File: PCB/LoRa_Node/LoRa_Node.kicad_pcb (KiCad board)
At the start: 2 copper layers, 90 x 34 mm, 65 parts, among them IC1 SPX5205M5-L/TR, IC2 SPX5205M5-L/TR, J1 Conn_01x04_Socket, J2 Conn_01x02_Pin, J3 UF.L, J4 2x5_2.00mm, J6 Conn_01x06_Socket, J7 Conn_01x03_Socket, SW1 SW_SPST, U1 BME280, U2 RFM95W-868S2, U3 STM32F103C8Tx, U4 SIM800L-CORE, Y1 12MHz, Y2 32.768kHz

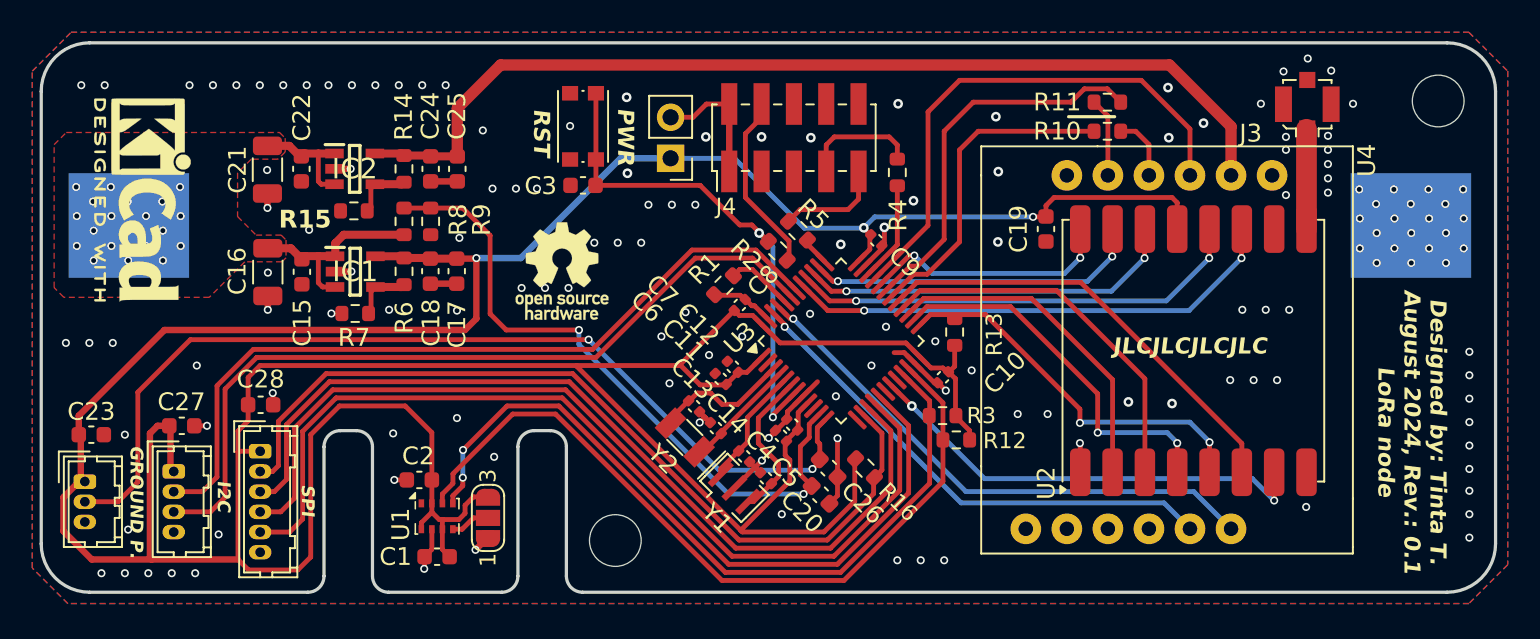
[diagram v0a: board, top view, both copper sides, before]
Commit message: Update
PCB: added pull-downs on IRQ pins, SW: stable EXTI, reliable measurements
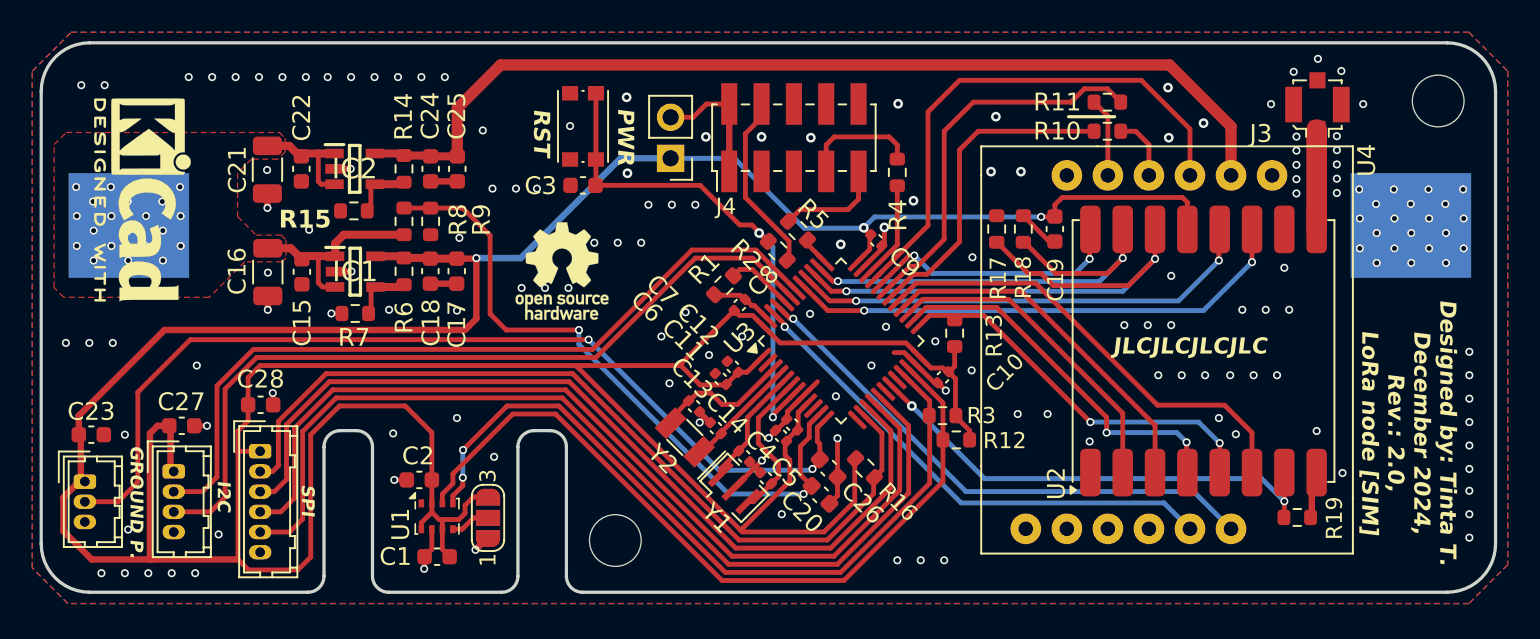
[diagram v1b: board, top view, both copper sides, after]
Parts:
- added R17: 10k, Resistor_SMD:R_0603_1608Metric, F.Cu at (164.8, 77.2)
- added R18: 10k, Resistor_SMD:R_0603_1608Metric, F.Cu at (166.5, 77.2)
- added R19: 10k, Resistor_SMD:R_0603_1608Metric, F.Cu at (183.4, 95.1)
- moved J3 0.63 mm to (184.7, 69.5)
- moved U2 0.63 mm to (177.6, 84.8)
- moved C19 0.55 mm to (168.4, 77.2)
- moved R13 0.08 mm to (162.2, 83.7)
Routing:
- net /DIO0: track 23.6 -> 35.2 mm
- net /DIO1: track 20.8 -> 28.2 mm
- net GND: track 41.3 -> 45.1 mm, vias 149 -> 161
- net /MOSI: track 23.5 -> 21.7 mm
- net /MISO: track 20.8 -> 19.6 mm
- net /DIO5: track 28.4 -> 29.6 mm
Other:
- board text added: "Designed by: Tinta T. December 2024, Rev.: 2.0, LoRa node [SIM]"
- board text removed: "Designed by: Tinta T. August 2024, Rev.: 0.1 LoRa node"

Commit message: Update
Humidity probe is rewired from the 3v3 to MCU pin for power
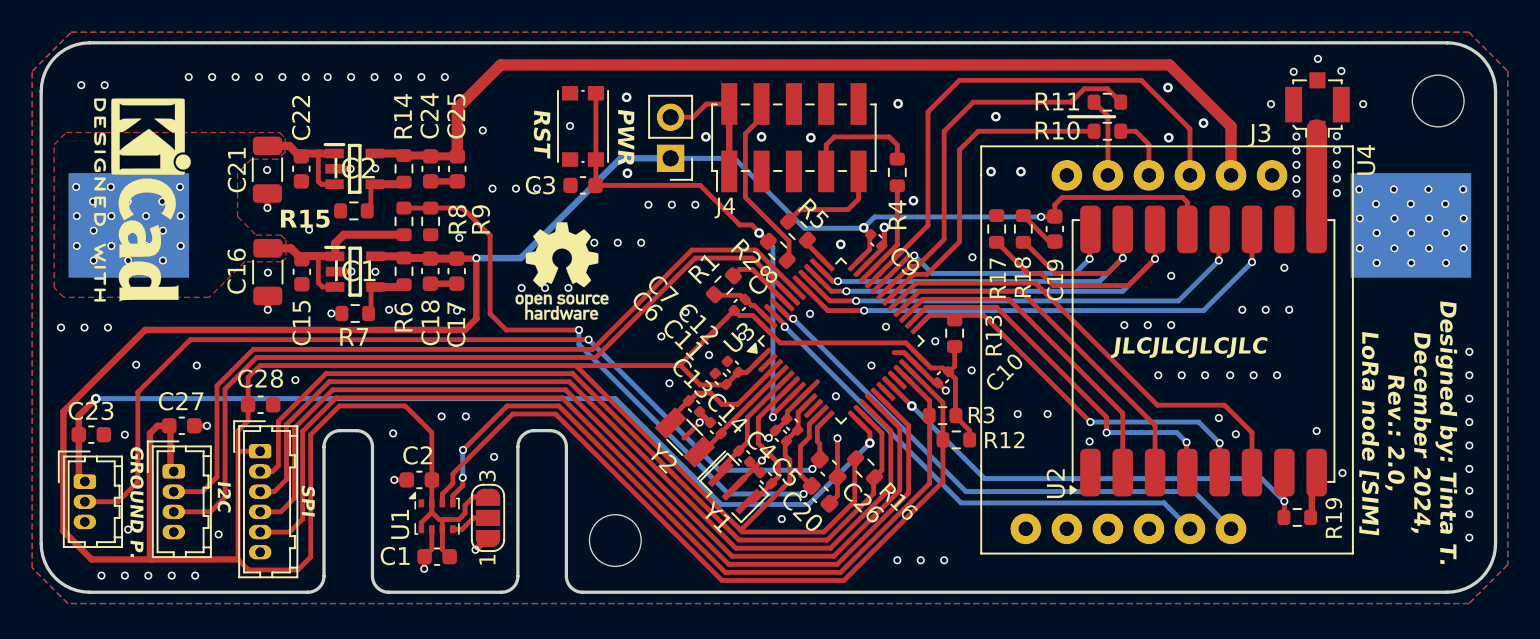
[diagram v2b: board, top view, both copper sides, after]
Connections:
- C23 pad 1: +3.3V -> /EHUM_PWR
- J7 pad 1: +3.3V -> /EHUM_PWR
- U3 pad 13: unconnected-(U3-PA3-Pad13) -> /EHUM_PWR
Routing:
- net /EHUM_PWR: track 0.00 -> 60.4 mm, vias 0 -> 2
- net GND: track 45.1 -> 45.8 mm, vias 161 -> 165

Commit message: README Update
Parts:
- added R20: 10k, Resistor_SMD:R_0603_1608Metric, F.Cu at (108.8, 88.4)
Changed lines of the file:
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@@
 		(tags "capacitor")
 		(property "Reference" "C23"
-			(at 0 -1.43 0)
+			(at -0.02132 -2.978681 0)
 			(layer "F.SilkS")
 			(effects
@@
 		)
 	)
+	(footprint "Resistor_SMD:R_0603_1608Metric"
+		(layer "F.Cu")
+		(at 108.77868 88.421319)
+		(descr "Resistor SMD 0603 (1608 Metric), square (rectangular) end terminal, IPC_7351 nominal, (Body size source: IPC-SM-782 page 72, https://www.pcb-3d.com/wordpress/wp-content/uploads/ipc-sm-782a_amendment_1_and_2.pdf), generated with kicad-footprint-generator")
+		(tags "resistor")
+		(property "Reference" "R20"
+			(at -0.1 -2.8 0)
+			(layer "F.SilkS")
+			(effects
+				(font
+					(size 1 1)
+					(thickness 0.15)
+				)
+			)
+		)
+		(property "Value" "10k"
+			(at 0 1.43 0)
+			(layer "F.Fab")
+			(effects
+				(font
+					(size 1 1)
+					(thickness 0.15)
+				)
+			)
+		)
+		(property "Footprint" "Resistor_SMD:R_0603_1608Metric"
+			(at 0 0 0)
+			(unlocked yes)
+			(layer "F.Fab")
+			(hide yes)
+			(effects
+				(font
+					(size 1.27 1.27)
+				)
+			)
+		)
+		(property "Datasheet" ""
+			(at 0 0 0)
+			(unlocked yes)
+			(layer "F.Fab")
+			(hide yes)
+			(effects
+				(font
+					(size 1.27 1.27)
+				)
+			)
+		)
+		(property "Description" ""
+			(at 0 0 0)
+			(unlocked yes)
+			(layer "F.Fab")
+			(hide yes)
+			(effects
+				(font
+					(size 1.27 1.27)
+				)
+			)
+		)
+		(property ki_fp_filters "R_*")
+		(sheetname "Root")
+		(sheetfile "LoRa_Node.kicad_sch")
+		(attr smd)
+		(fp_line
+			(start -0.237258 -0.5225)
+			(end 0.237258 -0.5225)
+			(stroke
+				(width 0.12)
+				(type solid)
+			)
+			(layer "F.SilkS")
+		)
+		(fp_line
+			(start -0.237258 0.5225)
+			(end 0.237258 0.5225)
+			(stroke
+				(width 0.12)
+				(type solid)
+			)
+			(layer "F.SilkS")
+		)
+		(fp_line
+			(start -1.48 -0.73)
+			(end 1.48 -0.73)
+			(stroke
+				(width 0.05)
+				(type solid)
+			)
+			(layer "F.CrtYd")
+		)
+		(fp_line
+			(start -1.48 0.73)
+			(end -1.48 -0.73)
+			(stroke
+				(width 0.05)
+				(type solid)
+			)
+			(layer "F.CrtYd")
+		)
+		(fp_line
+			(start 1.48 -0.73)
+			(end 1.48 0.73)
+			(stroke
+				(width 0.05)
+				(type solid)
+			)
+			(layer "F.CrtYd")
+		)
+		(fp_line
+			(start 1.48 0.73)
+			(end -1.48 0.73)
+			(stroke
+				(width 0.05)
+				(type solid)
+			)
+			(layer "F.CrtYd")
+		)
+		(fp_line
+			(start -0.8 -0.4125)
+			(end 0.8 -0.4125)
+			(stroke
+				(width 0.1)
+				(type solid)
+			)
+			(layer "F.Fab")
+		)
+		(fp_line
+			(start -0.8 0.4125)
+			(end -0.8 -0.4125)
+			(stroke
+				(width 0.1)
+				(type solid)
+			)
+			(layer "F.Fab")
+		)
+		(fp_line
+			(start 0.8 -0.4125)
+			(end 0.8 0.4125)
+			(stroke
+				(width 0.1)
+				(type solid)
+			)
+			(layer "F.Fab")
+		)
+		(fp_line
+			(start 0.8 0.4125)
+			(end -0.8 0.4125)
+			(stroke
+				(width 0.1)
+				(type solid)
+			)
+			(layer "F.Fab")
+		)
+		(fp_text user "${REFERENCE}"
+			(at 0 0 0)
+			(layer "F.Fab")
+			(effects
+				(font
+					(size 0.4 0.4)
+					(thickness 0.06)
+				)
+			)
+		)
+		(pad "1" smd roundrect
+			(at -0.825 0)
+			(size 0.8 0.95)
+			(layers "F.Cu" "F.Paste" "F.Mask")
+			(roundrect_rratio 0.25)
+			(net 62 "/EHUM_PWR")
+			(pintype "passive")
+		)
+		(pad "2" smd roundrect
+			(at 0.825 0)
+			(size 0.8 0.95)
+			(layers "F.Cu" "F.Paste" "F.Mask")
+			(roundrect_rratio 0.25)
+			(net 1 "GND")
+			(pintype "passive")
+		)
+		(model "${KICAD8_3DMODEL_DIR}/Resistor_SMD.3dshapes/R_0603_1608Metric.wrl"
+			(offset
+				(xyz 0 0 0)
+			)
+			(scale
+				(xyz 1 1 1)
+			)
+			(rotate
+				(xyz 0 0 0)
+			)
+		)
+	)
 	(footprint "Capacitor_SMD:C_0402_1005Metric"
 		(layer "F.Cu")
@@
 	)
 	(via
-		(at 109.82868 83.321319)
+		(at 109.67868 82.921319)
 		(size 0.5)
 		(drill 0.3)
@@
 	)
 	(via
-		(at 161.57868 97.721319)
+		(at 162.22868 97.271319)
 		(size 0.5)
 		(drill 0.3)
@@
 	)
 	(via
-		(at 106.92868 83.321319)
+		(at 106.77868 82.921319)
 		(size 0.5)
 		(drill 0.3)
@@
 	)
 	(via
-		(at 158.67868 97.721319)
+		(at 159.32868 97.271319)
 		(size 0.5)
 		(drill 0.3)
@@
 	)
 	(via
-		(at 160.12868 97.721319)
+		(at 160.77868 97.271319)
 		(size 0.5)
 		(drill 0.3)
@@
 	)
 	(via
-		(at 136.37868 74.721319)
+		(at 134.82868 71.121319)
 		(size 0.5)
 		(drill 0.3)
@@
 	)
 	(via
-		(at 108.37868 83.321319)
+		(at 108.22868 82.921319)
 		(size 0.5)
 		(drill 0.3)
@@
 	)
 	(via
-		(at 133.62868 74.721319)
+		(at 134.82868 73.871319)
 		(size 0.5)
 		(drill 0.3)
@@
 	)
 	(via
-		(at 135.07868 74.721319)
+		(at 134.82868 72.421319)
 		(size 0.5)
 		(drill 0.3)
@@
 	)
 	(segment
-		(start 107.07868 88.521319)
-		(end 112.12868 83.471319)
-		(width 0.4)
-		(layer "F.Cu")
-		(net 5)
-	)
-	(segment
 		(start 168.42868 75.721319)
 		(end 168.42868 76.446319)
@@
 	)
 	(segment
+		(start 112.52868 97.671319)
+		(end 108.82868 97.671319)
+		(width 0.4)
+		(layer "F.Cu")
+		(net 5)
+	)
+	(segment
 		(start 118.47868 88.125)
 		(end 118.50368 88.1)
@@
 	)
 	(segment
+		(start 111.27868 83.471319)
+		(end 131.92868 83.471319)
+		(width 0.4)
+		(layer "F.Cu")
+		(net 5)
+	)
+	(segment
 		(start 129.225 95.8)
 		(end 129.225 95.4)
@@
 	)
 	(segment
+		(start 108.82868 97.671319)
+		(end 107.07868 95.921319)
+		(width 0.4)
+		(layer "F.Cu")
+		(net 5)
+	)
+	(segment
 		(start 148.899857 82.571319)
 		(end 149.732231 82.571319)
@@
 	)
 	(segment
-		(start 132.62868 82.771319)
-		(end 132.62868 79.021319)
-		(width 0.4)
-		(layer "F.Cu")
-		(net 5)
-	)
-	(segment
-		(start 107.07868 95.921319)
-		(end 107.07868 88.521319)
+		(start 131.92868 83.471319)
+		(end 132.62868 82.771319)
 		(width 0.4)
 		(layer "F.Cu")
@@
 	)
 	(segment
+		(start 107.07868 95.921319)
+		(end 107.07868 87.671319)
+		(width 0.4)
+		(layer "F.Cu")
+		(net 5)
+	)
+	(segment
 		(start 156.60368 77.196319)
 		(end 157.039269 77.631908)
@@
 	)
 	(segment
-		(start 112.52868 97.671319)
-		(end 108.82868 97.671319)
-		(width 0.4)
-		(layer "F.Cu")
-		(net 5)
-	)
-	(segment
 		(start 152.489411 89.639411)
 		(end 151.739411 90.389411)
@@
 	)
 	(segment
+		(start 107.07868 87.671319)
+		(end 111.27868 83.471319)
+		(width 0.4)
+		(layer "F.Cu")
+		(net 5)
+	)
+	(segment
 		(start 152.02868 91.521319)
 		(end 152.02868 92.821319)
@@
 	)
 	(segment
-		(start 131.92868 83.471319)
-		(end 132.62868 82.771319)
+		(start 132.62868 82.771319)
+		(end 132.62868 79.021319)
 		(width 0.4)
 		(layer "F.Cu")
@@
 	)
 	(segment
-		(start 108.82868 97.671319)
-		(end 107.07868 95.921319)
-		(width 0.4)
-		(layer "F.Cu")
-		(net 5)
-	)
-	(segment
 		(start 176.62868 75.571319)
 		(end 176.32868 75.271319)
@@
 	)
 	(segment
-		(start 112.12868 83.471319)
-		(end 131.92868 83.471319)
-		(width 0.4)
-		(layer "F.Cu")
-		(net 5)
-	)
-	(segment
 		(start 148.589269 82.260731)
 		(end 148.899857 82.571319)
@@
 	)
 	(segment
-		(start 156.97868 90.471319)
-		(end 156.97868 89.821318)
-		(width 0.3)
+		(start 108.57868 87.621319)
+		(end 108.025 88.174999)
+		(width 0.4)
 		(layer "F.Cu")
 		(net 62)
 	)
 	(segment
-		(start 108.025 88.774999)
-		(end 108.025 89.95)
-		(width 0.4)
+		(start 156.97868 90.471319)
+		(end 156.97868 89.821318)
+		(width 0.3)
 		(layer "F.Cu")
 		(net 62)
 	)
 	(segment
-		(start 109.07868 87.721319)
-		(end 108.025 88.774999)
+		(start 108.02868 92.47868)
+		(end 108.02868 89.95368)
 		(width 0.4)
 		(layer "F.Cu")
@@
 	)
 	(segment
-		(start 108.02868 92.47868)
-		(end 108.02868 89.95368)
+		(start 108.025 88.174999)
+		(end 108.025 89.95)
 		(width 0.4)
 		(layer "F.Cu")
@@
 	)
 	(via
-		(at 109.07868 87.721319)
+		(at 108.57868 87.621319)
 		(size 0.6)
 		(drill 0.3)
@@
 	)
 	(segment
-		(start 109.07868 87.721319)
-		(end 141.22868 87.721319)
+		(start 141.12868 87.621319)
+		(end 147.77868 94.271319)
 		(width 0.3)
 		(layer "B.Cu")
@@
 	)
 	(segment
-		(start 153.17868 94.271319)
-		(end 156.97868 90.471319)
+		(start 108.57868 87.621319)
+		(end 141.12868 87.621319)
 		(width 0.3)
 		(layer "B.Cu")
@@
 	)
 	(segment
-		(start 141.22868 87.721319)
-		(end 147.77868 94.271319)
+		(start 153.17868 94.271319)
+		(end 156.97868 90.471319)
 		(width 0.3)
 		(layer "B.Cu")

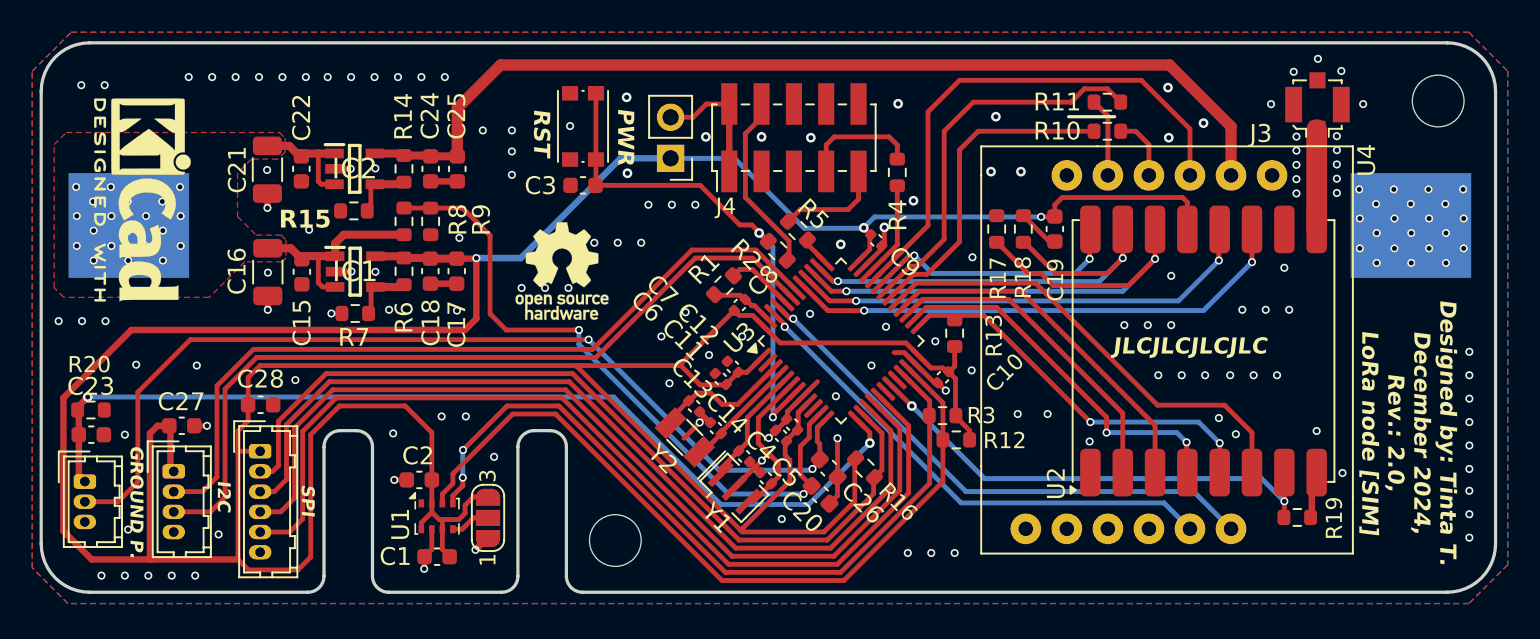
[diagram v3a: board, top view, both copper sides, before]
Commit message: Update:
4V bus update (step-up converter)
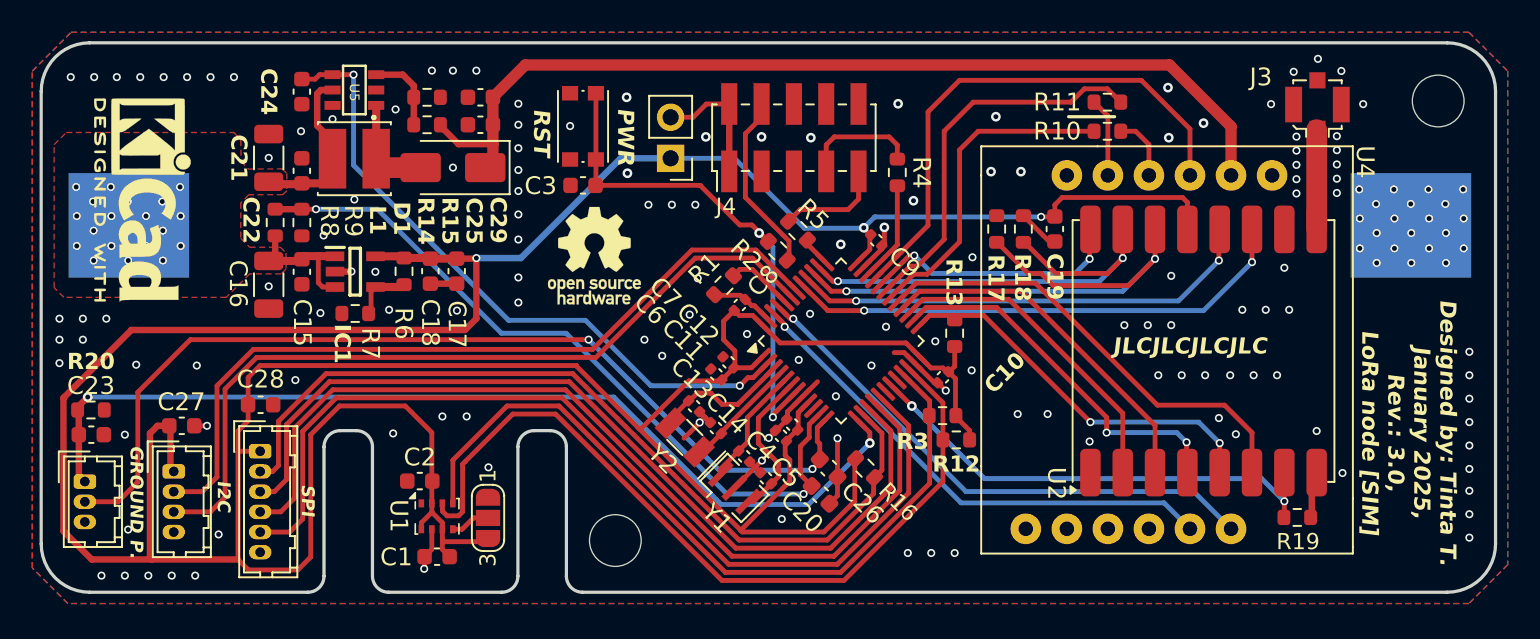
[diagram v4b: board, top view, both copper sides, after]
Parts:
- removed IC2: SPX5205M5-L/TR, SPX5205M5-L-3-3_TR:SOT95P280X145-5N
- added C29: 10nF, Capacitor_SMD:C_0603_1608Metric, F.Cu at (132.9, 70.8)
- added D1: SS24, Diode_SMD:D_SMA, F.Cu at (131.2, 73.4)
- added L1: 4.7uH, Inductor_SMD:L_Cenker_CKCS4020, F.Cu at (125.1, 72.9)
- added U5: SX1308, SX1308:SOT-23-6, F.Cu at (125.1, 68.6)
- C24: value 1uF -> 10nF
- C25: value 10nF -> 1uF
- R14: value 22k -> 20k
- R15: value 10k -> 3k2
- R8, R9: value 10k -> 500k
- moved C24 9.29 mm to (121.8, 68.7)
- moved R15 8.36 mm to (129.6, 69.1), turned to 180 degrees
- moved R8 7.97 mm to (120.2, 76.8)
- moved R9 7.97 mm to (121.8, 76.8)
- moved C25 4.65 mm to (132.9, 69.1), turned to 180 degrees
- moved R14 3.08 mm to (129.6, 70.8), turned to 0 degrees
- moved REF** 2.21 mm to (139.9, 78.9)
- moved C16 0.78 mm to (119.8, 80.7)
- moved C21 0.73 mm to (119.8, 72.8), turned to 90 degrees
- moved C6 0.39 mm to (147.5, 86.2)
- moved C7 0.39 mm to (148.2, 85.5)
- moved C22 0.12 mm to (121.8, 73.6), turned to 90 degrees
- moved C2 0.08 mm to (129.1, 92.8)
- turned JP1 to -90 degrees
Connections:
- C24 pad 1: +4V -> /BOOST_EN
- U3 pad 2: unconnected-(U3-PC13-Pad2) -> /BOOST_EN
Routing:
- net /BOOST_EN: track 0.00 -> 40.8 mm, vias 0 -> 2
- net GND: track 45.8 -> 38.8 mm, vias 165 -> 163
- net Net-(D1-A): track 0.00 -> 6.28 mm
- net /AN_BAT: track 41.4 -> 45.9 mm
- net +3.3V: track 264.4 -> 260.6 mm
- net +4V: track 61.8 -> 59.4 mm
- net /SDA: track 48.6 -> 50.6 mm
- net +Vbat: track 20.0 -> 18.2 mm
- net Net-(U5-FB): track 3.70 -> 5.03 mm
- net /SCL: vias 2 -> 0
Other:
- board text added: "Designed by: Tinta T. January 2025, Rev.: 3.0, LoRa node [SIM]"
- board text removed: "Designed by: Tinta T. December 2024, Rev.: 2.0, LoRa node [SIM]"
